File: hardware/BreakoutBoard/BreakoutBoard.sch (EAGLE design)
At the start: 38 parts, among them J1 CON-71741-2184-TOP, J10 CON-2X3-RASTER, J11 CON-2X3-RASTER, J12 CON-2X3-RASTER, J13 CON-2X4-RASTER, J2 CON-71741-2184-BOT, J3 CON-2X4-RASTER, J4 CON-2X10-RASTER, J5 CON-2X3-RASTER, J6 CON-2X3-RASTER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

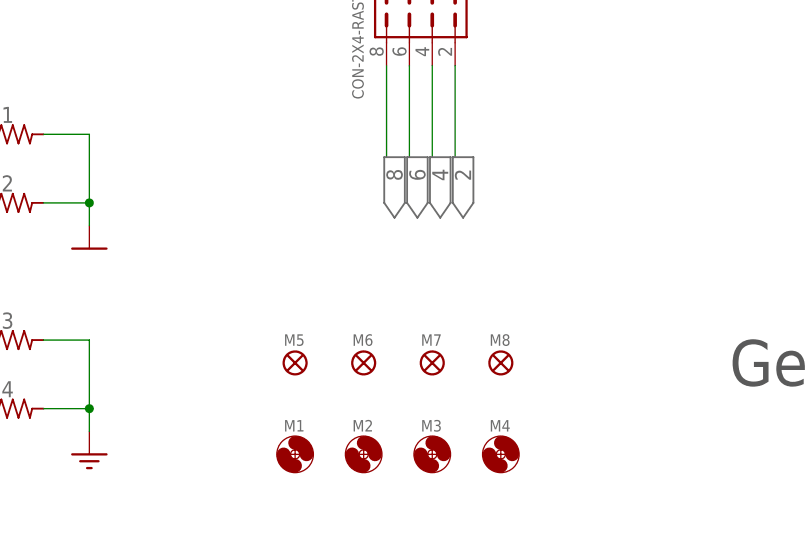
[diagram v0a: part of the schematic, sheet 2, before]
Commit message: - Fiducials in both sides
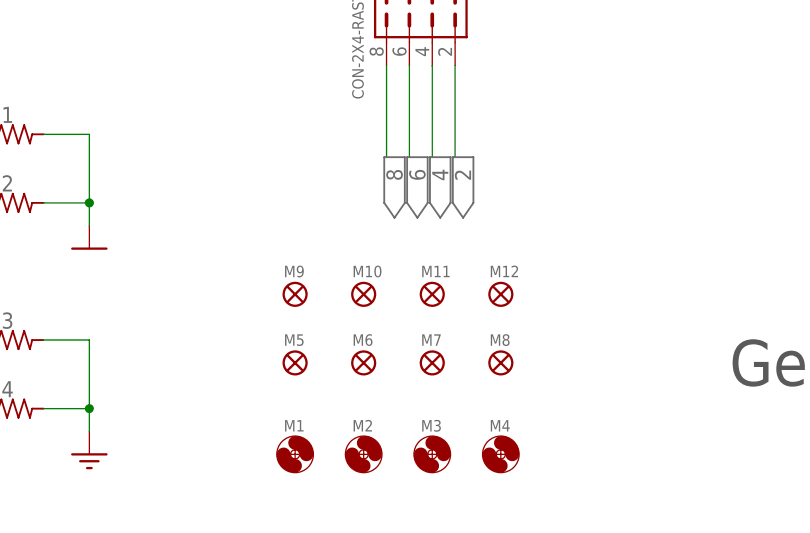
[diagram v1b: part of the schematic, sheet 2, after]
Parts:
- added M10, M11, M12, M9: FIDUCIAL1X2, powerboard:FIDUCIAL1X2
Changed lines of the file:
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@@
 <part name="FRAME1" library="BreakoutBoard" deviceset="FRAME-LETTER" device=""/>
 <part name="FRAME2" library="BreakoutBoard" deviceset="FRAME-LETTER" device=""/>
+<part name="M9" library="powerboard" deviceset="FIDUCIAL" device="1X2"/>
+<part name="M10" library="powerboard" deviceset="FIDUCIAL" device="1X2"/>
+<part name="M11" library="powerboard" deviceset="FIDUCIAL" device="1X2"/>
+<part name="M12" library="powerboard" deviceset="FIDUCIAL" device="1X2"/>
 </parts>
 <sheets>
@@
 <instance part="FRAME2" gate="G$1" x="0" y="0"/>
 <instance part="FRAME2" gate="G$2" x="147.32" y="0"/>
+<instance part="M9" gate="G$1" x="132.08" y="30.48"/>
+<instance part="M10" gate="G$1" x="139.7" y="30.48"/>
+<instance part="M11" gate="G$1" x="147.32" y="30.48"/>
+<instance part="M12" gate="G$1" x="154.94" y="30.48"/>
 </instances>
 <busses>
